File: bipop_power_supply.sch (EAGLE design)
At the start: 22 parts, among them IC1 LM1117MP-3.3, IC2 LM1117MP-5.0

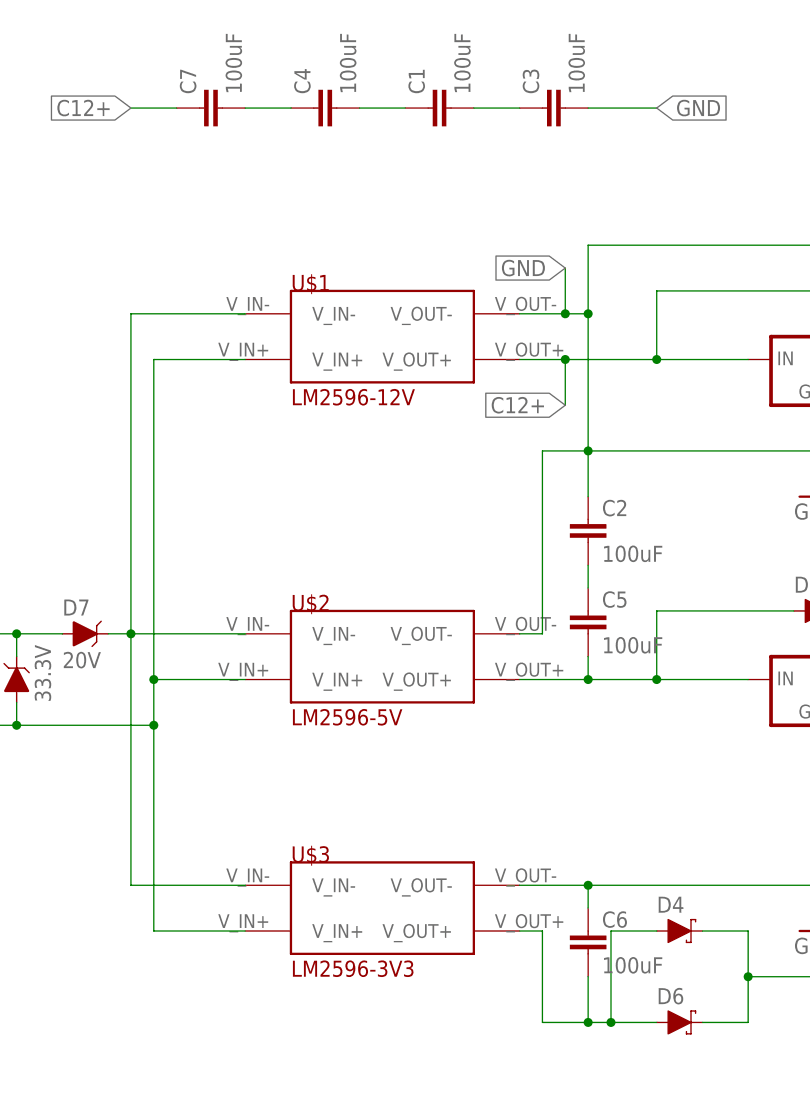
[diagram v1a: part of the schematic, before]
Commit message: plytka z kondensatorami i diodami +pdfy
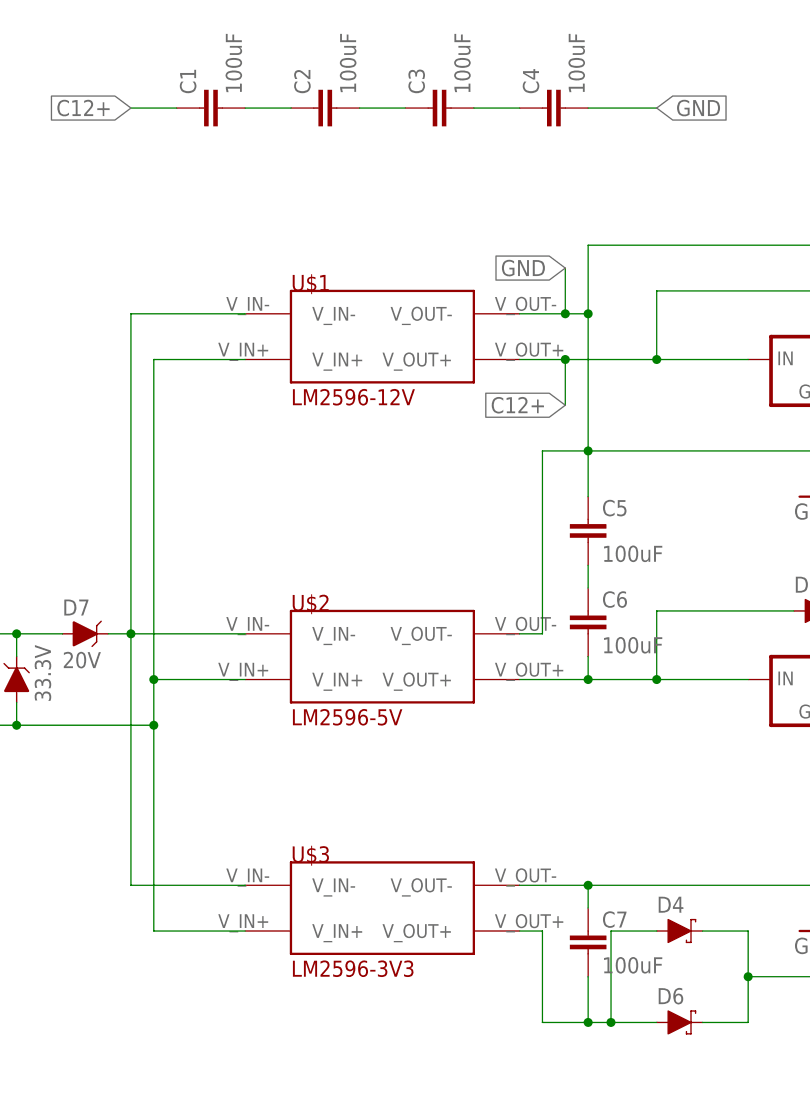
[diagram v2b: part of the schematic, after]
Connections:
- removed net N$10: C1.1, C4.2
- removed net N$12: C1.2, C3.1
- new net N$2: C2.2, C3.1
- new net N$6: C3.2, C4.1
- net C12+: now also C1.1; no longer C7.1
- net GND: now also C4.2, C5.1, C7.1; no longer C2.1, C3.2, C6.1
- net N$4: now also C6.2; no longer C5.2
- net N$7: now also C7.2; no longer C6.2
- net N$8: now also C5.2, C6.1; no longer C2.2, C5.1
- net N$9: now also C1.2, C2.1; no longer C4.1, C7.2
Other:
- moved on the sheet: C1, C2, C3, C4, C5, C6, C7
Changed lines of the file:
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@@
 <part name="C1" library="rcl" library_urn="urn:adsk.eagle:library:334" deviceset="C-EU" device="C0805" package3d_urn="urn:adsk.eagle:package:23617/2" value="100uF"/>
 <part name="D8" library="SparkFun-DiscreteSemi" deviceset="DIODE-ZENER" device="-MM3Z3V3T1G" value="33.3V"/>
+<part name="C2" library="rcl" library_urn="urn:adsk.eagle:library:334" deviceset="C-EU" device="C0805" package3d_urn="urn:adsk.eagle:package:23617/2" value="100uF"/>
+<part name="C3" library="rcl" library_urn="urn:adsk.eagle:library:334" deviceset="C-EU" device="C0805" package3d_urn="urn:adsk.eagle:package:23617/2" value="100uF"/>
 <part name="C4" library="rcl" library_urn="urn:adsk.eagle:library:334" deviceset="C-EU" device="C0805" package3d_urn="urn:adsk.eagle:package:23617/2" value="100uF"/>
 <part name="C5" library="rcl" library_urn="urn:adsk.eagle:library:334" deviceset="C-EU" device="C0805" package3d_urn="urn:adsk.eagle:package:23617/2" value="100uF"/>
 <part name="C6" library="rcl" library_urn="urn:adsk.eagle:library:334" deviceset="C-EU" device="C0805" package3d_urn="urn:adsk.eagle:package:23617/2" value="100uF"/>
-<part name="C2" library="rcl" library_urn="urn:adsk.eagle:library:334" deviceset="C-EU" device="C0805" package3d_urn="urn:adsk.eagle:package:23617/2" value="100uF"/>
-<part name="C3" library="rcl" library_urn="urn:adsk.eagle:library:334" deviceset="C-EU" device="C0805" package3d_urn="urn:adsk.eagle:package:23617/2" value="100uF"/>
 <part name="C7" library="rcl" library_urn="urn:adsk.eagle:library:334" deviceset="C-EU" device="C0805" package3d_urn="urn:adsk.eagle:package:23617/2" value="100uF"/>
 </parts>
@@
 <instance part="FRAME1" gate="G$2" x="48.26" y="-101.6"/>
 <instance part="D7" gate="G$1" x="-5.08" y="22.86"/>
-<instance part="C1" gate="G$1" x="33.02" y="81.28" rot="R90"/>
+<instance part="C1" gate="G$1" x="7.62" y="81.28" rot="R90"/>
 <instance part="D8" gate="G$1" x="-12.7" y="17.78" rot="R90"/>
-<instance part="C4" gate="G$1" x="20.32" y="81.28" rot="R90"/>
-<instance part="C5" gate="G$1" x="50.8" y="25.4"/>
-<instance part="C6" gate="G$1" x="50.8" y="-10.16"/>
-<instance part="C2" gate="G$1" x="50.8" y="35.56"/>
-<instance part="C3" gate="G$1" x="45.72" y="81.28" rot="R90"/>
-<instance part="C7" gate="G$1" x="7.62" y="81.28" rot="R90"/>
+<instance part="C2" gate="G$1" x="20.32" y="81.28" rot="R90"/>
+<instance part="C3" gate="G$1" x="33.02" y="81.28" rot="R90"/>
+<instance part="C4" gate="G$1" x="45.72" y="81.28" rot="R90"/>
+<instance part="C5" gate="G$1" x="50.8" y="35.56"/>
+<instance part="C6" gate="G$1" x="50.8" y="25.4"/>
+<instance part="C7" gate="G$1" x="50.8" y="-10.16"/>
 </instances>
 <busses>
@@
 <wire x1="119.38" y1="30.48" x2="119.38" y2="43.18" width="0.1524" layer="91"/>
 <pinref part="IC2" gate="G$1" pin="GND"/>
-<pinref part="C2" gate="G$1" pin="1"/>
 <wire x1="50.8" y1="38.1" x2="50.8" y2="43.18" width="0.1524" layer="91"/>
 <junction x="50.8" y="43.18"/>
@@
 <junction x="48.26" y="58.42"/>
 <label x="48.26" y="63.5" size="1.778" layer="95" rot="R180" xref="yes"/>
+<pinref part="C5" gate="G$1" pin="1"/>
 </segment>
 <segment>
@@
 <pinref part="U$3" gate="G$1" pin="V_OUT-"/>
 <pinref part="IC1" gate="G$1" pin="GND"/>
-<pinref part="C6" gate="G$1" pin="1"/>
 <wire x1="50.8" y1="-7.62" x2="50.8" y2="-5.08" width="0.1524" layer="91"/>
 <junction x="50.8" y="-5.08"/>
-</segment>
-<segment>
-<pinref part="C3" gate="G$1" pin="2"/>
+<pinref part="C7" gate="G$1" pin="1"/>
+</segment>
+<segment>
 <wire x1="50.8" y1="81.28" x2="58.42" y2="81.28" width="0.1524" layer="91"/>
 <label x="58.42" y="81.28" size="1.778" layer="95" xref="yes"/>
+<pinref part="C4" gate="G$1" pin="2"/>
 </segment>
 </net>
@@
 <wire x1="58.42" y1="-20.32" x2="53.34" y2="-20.32" width="0.1524" layer="91"/>
 <wire x1="53.34" y1="-20.32" x2="53.34" y2="-10.16" width="0.1524" layer="91"/>
-<pinref part="C6" gate="G$1" pin="2"/>
 <wire x1="50.8" y1="-15.24" x2="50.8" y2="-20.32" width="0.1524" layer="91"/>
 <wire x1="50.8" y1="-20.32" x2="53.34" y2="-20.32" width="0.1524" layer="91"/>
@@
 <wire x1="45.72" y1="-20.32" x2="50.8" y2="-20.32" width="0.1524" layer="91"/>
 <junction x="50.8" y="-20.32"/>
+<pinref part="C7" gate="G$1" pin="2"/>
 </segment>
 </net>
@@
 <pinref part="U$2" gate="G$1" pin="V_OUT+"/>
 <pinref part="IC1" gate="G$1" pin="IN"/>
-<pinref part="C5" gate="G$1" pin="2"/>
 <wire x1="50.8" y1="20.32" x2="50.8" y2="17.78" width="0.1524" layer="91"/>
 <junction x="50.8" y="17.78"/>
+<pinref part="C6" gate="G$1" pin="2"/>
 </segment>
 </net>
@@
 <net name="N$8" class="0">
 <segment>
-<pinref part="C5" gate="G$1" pin="1"/>
-<pinref part="C2" gate="G$1" pin="2"/>
 <wire x1="50.8" y1="27.94" x2="50.8" y2="30.48" width="0.1524" layer="91"/>
+<pinref part="C5" gate="G$1" pin="2"/>
+<pinref part="C6" gate="G$1" pin="1"/>
 </segment>
 </net>
 <net name="C12+" class="0">
 <segment>
-<pinref part="C7" gate="G$1" pin="1"/>
 <wire x1="5.08" y1="81.28" x2="0" y2="81.28" width="0.1524" layer="91"/>
 <label x="0" y="81.28" size="1.778" layer="95" rot="R180" xref="yes"/>
+<pinref part="C1" gate="G$1" pin="1"/>
 </segment>
 <segment>
@@
 <net name="N$9" class="0">
 <segment>
-<pinref part="C7" gate="G$1" pin="2"/>
+<wire x1="12.7" y1="81.28" x2="17.78" y2="81.28" width="0.1524" layer="91"/>
+<pinref part="C1" gate="G$1" pin="2"/>
+<pinref part="C2" gate="G$1" pin="1"/>
+</segment>
+</net>
+<net name="N$2" class="0">
+<segment>
+<pinref part="C2" gate="G$1" pin="2"/>
+<pinref part="C3" gate="G$1" pin="1"/>
+<wire x1="25.4" y1="81.28" x2="30.48" y2="81.28" width="0.1524" layer="91"/>
+</segment>
+</net>
+<net name="N$6" class="0">
+<segment>
 <pinref part="C4" gate="G$1" pin="1"/>
-<wire x1="12.7" y1="81.28" x2="17.78" y2="81.28" width="0.1524" layer="91"/>
-</segment>
-</net>
-<net name="N$10" class="0">
-<segment>
-<pinref part="C4" gate="G$1" pin="2"/>
-<pinref part="C1" gate="G$1" pin="1"/>
-<wire x1="25.4" y1="81.28" x2="30.48" y2="81.28" width="0.1524" layer="91"/>
-</segment>
-</net>
-<net name="N$12" class="0">
-<segment>
-<pinref part="C1" gate="G$1" pin="2"/>
-<pinref part="C3" gate="G$1" pin="1"/>
-<wire x1="38.1" y1="81.28" x2="43.18" y2="81.28" width="0.1524" layer="91"/>
-</segment>
-</net>
+<pinref part="C3" gate="G$1" pin="2"/>
+<wire x1="43.18" y1="81.28" x2="38.1" y2="81.28" width="0.1524" layer="91"/>
+</segment>
+</net>

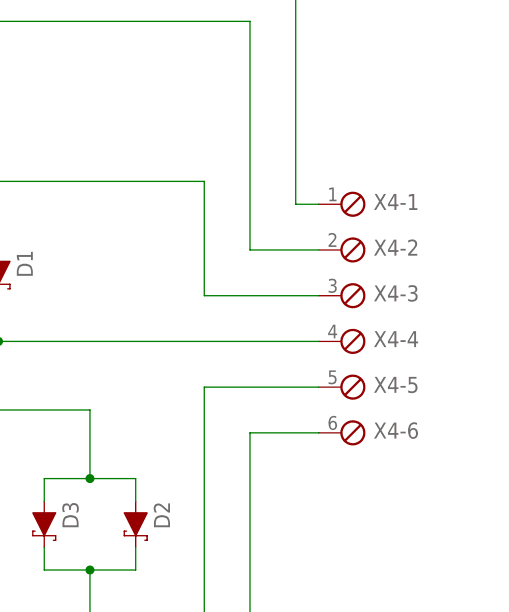
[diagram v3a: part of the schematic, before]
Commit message: Changed connector in bipop_power_supply board, modified routing and board's dimensions.
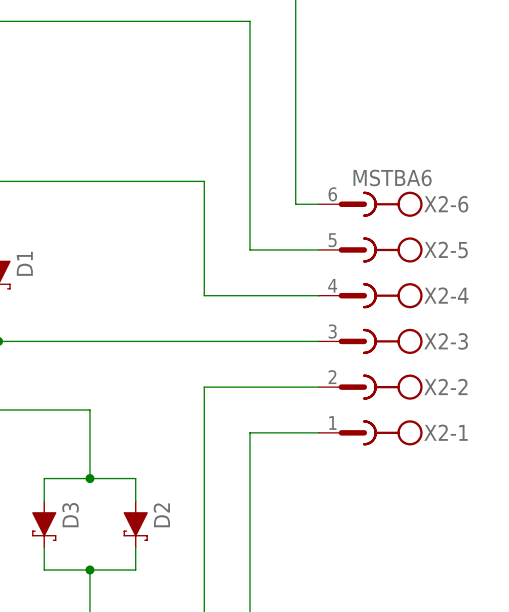
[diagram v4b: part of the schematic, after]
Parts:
- removed X4: (no value), con-phoenix-254:MPT6
- added X2: MSTBA6, con-phoenix-508:MSTBA6
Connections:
- net C12+: now also X2-5.1; no longer X4-2.1
- net GND: now also X2-2.1, X2-4.1, X2-6.1; no longer X4-1.1, X4-3.1, X4-5.1
- net N$11: now also X2-1.1; no longer X4-6.1
- net N$16: now also X2-3.1; no longer X4-4.1
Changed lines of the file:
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@@
 <?xml version="1.0" encoding="utf-8"?>
 <!DOCTYPE eagle SYSTEM "eagle.dtd">
-<eagle version="8.3.2">
+<eagle version="8.5.1">
 <drawing>
 <settings>
@@
 <part name="GND1" library="supply1" library_urn="urn:adsk.eagle:library:371" deviceset="GND" device=""/>
 <part name="GND2" library="supply1" library_urn="urn:adsk.eagle:library:371" deviceset="GND" device=""/>
-<part name="X4" library="con-phoenix-254" library_urn="urn:adsk.eagle:library:172" deviceset="MPT6" device="" package3d_urn="urn:adsk.eagle:package:9318/1"/>
 <part name="X1" library="con-phoenix-254" library_urn="urn:adsk.eagle:library:172" deviceset="MPT2" device="" package3d_urn="urn:adsk.eagle:package:9320/1"/>
 <part name="U$1" library="lustro_pcb" deviceset="LM2596-" device="12V"/>
@@
 <part name="C7" library="rcl" library_urn="urn:adsk.eagle:library:334" deviceset="C-EU" device="C0805" package3d_urn="urn:adsk.eagle:package:23617/2" value="100uF"/>
 <part name="C4" library="rcl" library_urn="urn:adsk.eagle:library:334" deviceset="C-EU" device="C0805" package3d_urn="urn:adsk.eagle:package:23617/2" value="100uF"/>
+<part name="X2" library="con-phoenix-508" library_urn="urn:adsk.eagle:library:176" deviceset="MSTBA6" device="" package3d_urn="urn:adsk.eagle:package:9616/1"/>
 </parts>
 <sheets>
@@
 <instance part="GND1" gate="1" x="76.2" y="38.1"/>
 <instance part="GND2" gate="1" x="76.2" y="-10.16"/>
-<instance part="X4" gate="-1" x="134.62" y="40.64"/>
-<instance part="X4" gate="-2" x="134.62" y="35.56"/>
-<instance part="X4" gate="-3" x="134.62" y="30.48"/>
-<instance part="X4" gate="-4" x="134.62" y="25.4"/>
-<instance part="X4" gate="-5" x="134.62" y="20.32"/>
-<instance part="X4" gate="-6" x="134.62" y="15.24"/>
 <instance part="X1" gate="-1" x="-17.78" y="12.7" rot="R180"/>
 <instance part="X1" gate="-2" x="-17.78" y="22.86" rot="R180"/>
@@
 <instance part="C7" gate="G$1" x="50.8" y="-10.16"/>
 <instance part="C4" gate="G$1" x="45.72" y="81.28" rot="R90"/>
+<instance part="X2" gate="-1" x="137.16" y="15.24" rot="R180"/>
+<instance part="X2" gate="-2" x="137.16" y="20.32" rot="R180"/>
+<instance part="X2" gate="-3" x="137.16" y="25.4" rot="R180"/>
+<instance part="X2" gate="-4" x="137.16" y="30.48" rot="R180"/>
+<instance part="X2" gate="-5" x="137.16" y="35.56" rot="R180"/>
+<instance part="X2" gate="-6" x="137.16" y="40.64" rot="R180"/>
 </instances>
 <busses>
@@
 <wire x1="76.2" y1="43.18" x2="50.8" y2="43.18" width="0.1524" layer="91"/>
 <wire x1="119.38" y1="43.18" x2="76.2" y2="43.18" width="0.1524" layer="91"/>
-<pinref part="X4" gate="-1" pin="1"/>
 <wire x1="132.08" y1="40.64" x2="129.54" y2="40.64" width="0.1524" layer="91"/>
 <wire x1="129.54" y1="40.64" x2="129.54" y2="66.04" width="0.1524" layer="91"/>
-<pinref part="X4" gate="-3" pin="1"/>
 <wire x1="132.08" y1="30.48" x2="119.38" y2="30.48" width="0.1524" layer="91"/>
 <wire x1="119.38" y1="30.48" x2="119.38" y2="43.18" width="0.1524" layer="91"/>
@@
 <label x="48.26" y="63.5" size="1.778" layer="95" rot="R180" xref="yes"/>
 <pinref part="C5" gate="G$1" pin="1"/>
+<pinref part="X2" gate="-4" pin="1"/>
+<pinref part="X2" gate="-6" pin="1"/>
 </segment>
 <segment>
 <pinref part="GND2" gate="1" pin="GND"/>
 <wire x1="76.2" y1="-7.62" x2="76.2" y2="-5.08" width="0.1524" layer="91"/>
-<pinref part="X4" gate="-5" pin="1"/>
 <wire x1="76.2" y1="-5.08" x2="76.2" y2="10.16" width="0.1524" layer="91"/>
 <wire x1="132.08" y1="20.32" x2="119.38" y2="20.32" width="0.1524" layer="91"/>
@@
 <junction x="50.8" y="-5.08"/>
 <pinref part="C7" gate="G$1" pin="1"/>
+<pinref part="X2" gate="-2" pin="1"/>
 </segment>
 <segment>
@@
 <net name="N$16" class="0">
 <segment>
-<pinref part="X4" gate="-4" pin="1"/>
 <pinref part="D1" gate="G$1" pin="C"/>
 <wire x1="96.52" y1="25.4" x2="96.52" y2="30.48" width="0.1524" layer="91"/>
@@
 <wire x1="78.74" y1="25.4" x2="96.52" y2="25.4" width="0.1524" layer="91"/>
 <junction x="96.52" y="25.4"/>
+<pinref part="X2" gate="-3" pin="1"/>
 </segment>
 </net>
@@
 <wire x1="106.68" y1="0" x2="101.6" y2="0" width="0.1524" layer="91"/>
 <wire x1="101.6" y1="0" x2="101.6" y2="2.54" width="0.1524" layer="91"/>
-<pinref part="X4" gate="-6" pin="1"/>
 <wire x1="132.08" y1="15.24" x2="124.46" y2="15.24" width="0.1524" layer="91"/>
 <wire x1="124.46" y1="15.24" x2="124.46" y2="-15.24" width="0.1524" layer="91"/>
@@
 <junction x="106.68" y="0"/>
 <junction x="106.68" y="-15.24"/>
+<pinref part="X2" gate="-1" pin="1"/>
 </segment>
 </net>
@@
 <wire x1="58.42" y1="60.96" x2="58.42" y2="53.34" width="0.1524" layer="91"/>
 <wire x1="68.58" y1="53.34" x2="58.42" y2="53.34" width="0.1524" layer="91"/>
-<pinref part="X4" gate="-2" pin="1"/>
 <wire x1="132.08" y1="35.56" x2="124.46" y2="35.56" width="0.1524" layer="91"/>
 <wire x1="124.46" y1="35.56" x2="124.46" y2="60.96" width="0.1524" layer="91"/>
@@
 <junction x="48.26" y="53.34"/>
 <label x="48.26" y="48.26" size="1.778" layer="95" rot="R180" xref="yes"/>
-</segment>
-</net>
+<pinref part="X2" gate="-5" pin="1"/>
+</segment>
+</net>
